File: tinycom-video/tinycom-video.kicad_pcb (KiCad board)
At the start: 2 copper layers, 45.2 x 45.2 mm, 47 parts, among them J1 MICRO_SD_HINGE, P1 CONN_02X10, P2 CONN_02X10, P4 USB_OTG, U1 SY8008BAAC, U2 AXP209, U3 SY8008BAAC, U4 RTL8188, U5 rainsun-antenna

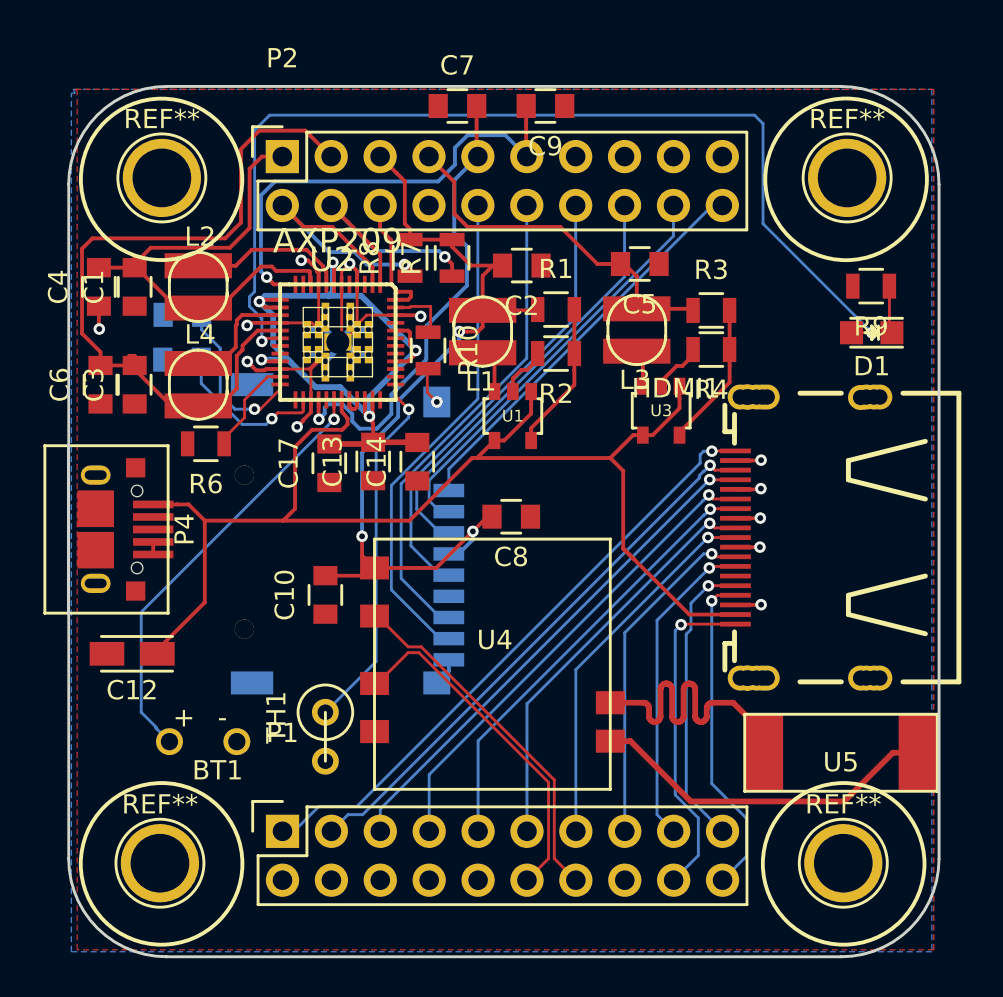
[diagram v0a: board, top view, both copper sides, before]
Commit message: move hdmi
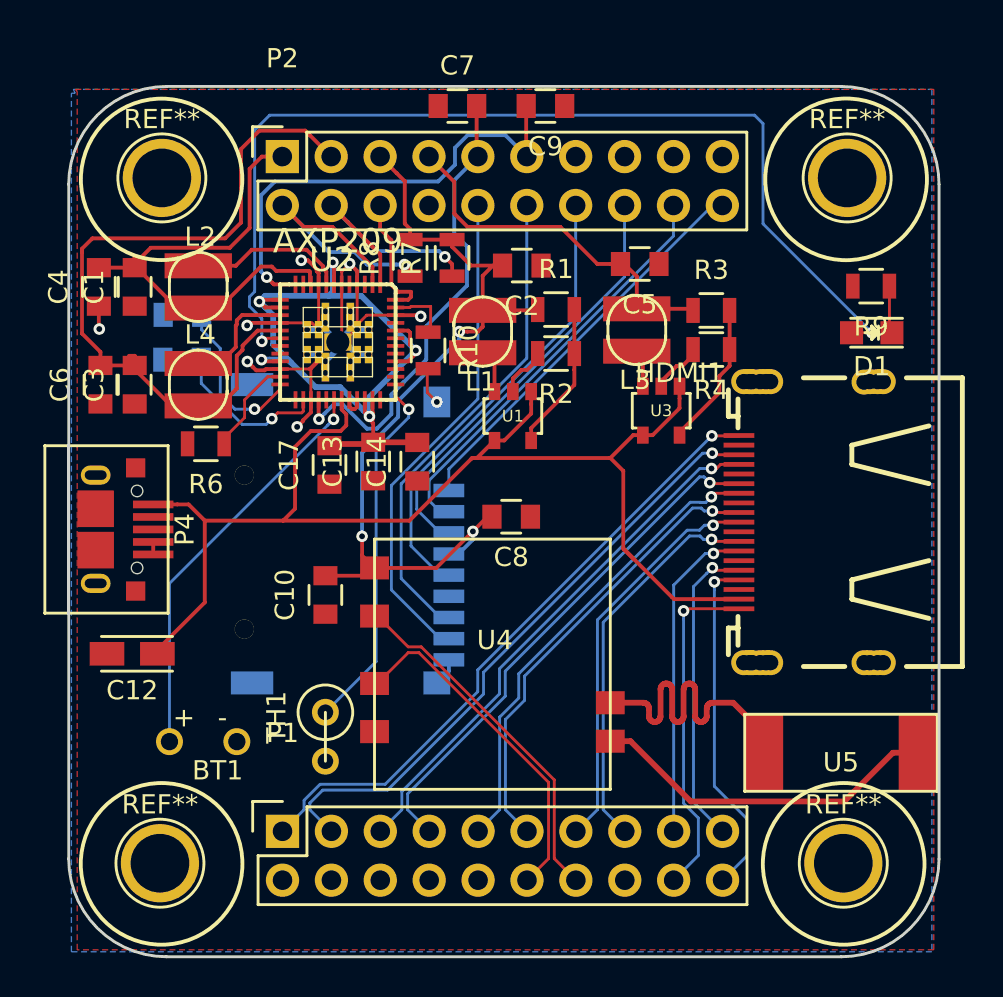
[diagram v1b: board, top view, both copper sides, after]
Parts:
- moved HDMI1 0.82 mm to (164.8, 101.9)
- moved C17 0.09 mm to (138.0, 98.9)
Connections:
- net HTX0N renamed HTX0_N
- net HTX0P renamed HTX0_P
- net HTX1N renamed HTX1_N
- net HTX1P renamed HTX1_P
- net HTX2N renamed HTX2_N
- net HTX2P renamed HTX2_P
- net HTXCN renamed HTXC_N
- net HTXCP renamed HTXC_P
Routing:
- net GND: track 59.0 -> 52.4 mm, vias 13 -> 8
- net HTX2_N: track 29.0 -> 32.4 mm
- net HTXC_N: track 17.8 -> 20.3 mm
- net HTX1_N: track 25.0 -> 27.3 mm
- net HTX0_N: track 21.4 -> 23.7 mm
- net HTXC_P: track 19.5 -> 20.9 mm
- net Net-(BT1-Pad1): track 22.5 -> 21.3 mm
- net HTX2_P: track 32.0 -> 33.2 mm
- net HTX1_P: track 26.7 -> 27.8 mm
- net HTX0_P: track 23.1 -> 24.1 mm
- net HSDA: track 17.1 -> 18.0 mm
- net HCSL: track 15.4 -> 16.2 mm
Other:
- net class Default: trace_width 0.2 -> 0.15

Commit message: update base
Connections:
- net MICIN1 renamed Net-(P1-Pad16)
- P1 pad 10: UD0_N -> UD1_N
- P1 pad 12: UD1_P -> Net-(P1-Pad12)
- P1 pad 14: UD1_N -> Net-(P1-Pad14)
- P1 pad 4: UART1_TX -> UD0_P
- P1 pad 6: UART1_RX -> UD0_N
- P1 pad 8: UD0_P -> UD1_P
- P2 pad 15: Net-(P2-Pad15) -> UART1_RX
- P2 pad 17: Net-(P2-Pad17) -> UART1_TX
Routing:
- net UD1_N: track 18.5 -> 16.7 mm
- net UD1_P: track 18.0 -> 16.3 mm

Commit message: vid usb
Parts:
- moved C12 6.78 mm to (132.7, 104.0), turned to 270 degrees
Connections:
- P4 pad 2: Net-(P4-Pad2) -> UD0_N
- P4 pad 3: Net-(P4-Pad3) -> UD0_P
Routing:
- net UD0_N: track 0.00 -> 27.1 mm
- net UD0_P: track 0.00 -> 26.5 mm
- net +5V: track 65.9 -> 59.7 mm
